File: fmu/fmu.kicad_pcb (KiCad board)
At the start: 4 copper layers, 103 parts, among them IC2 EFR32FG28B320F1024IM68-AR, J1 1054500101, J4 2213932-3, J5 2213932-3, J6 2213932-3, J7 2213932-3, U10 DMN3016LK3-13, U11 BQ7694203PFBR, U3 BNO055, U4 MCF8316A1VRGFR, U5 MCF8316A1VRGFR, U6 MCF8316A1VRGFR, U7 MCF8316A1VRGFR, U8 AR0130CSSC00SPBA0-DR, U9 MAX20075ATCA/V+

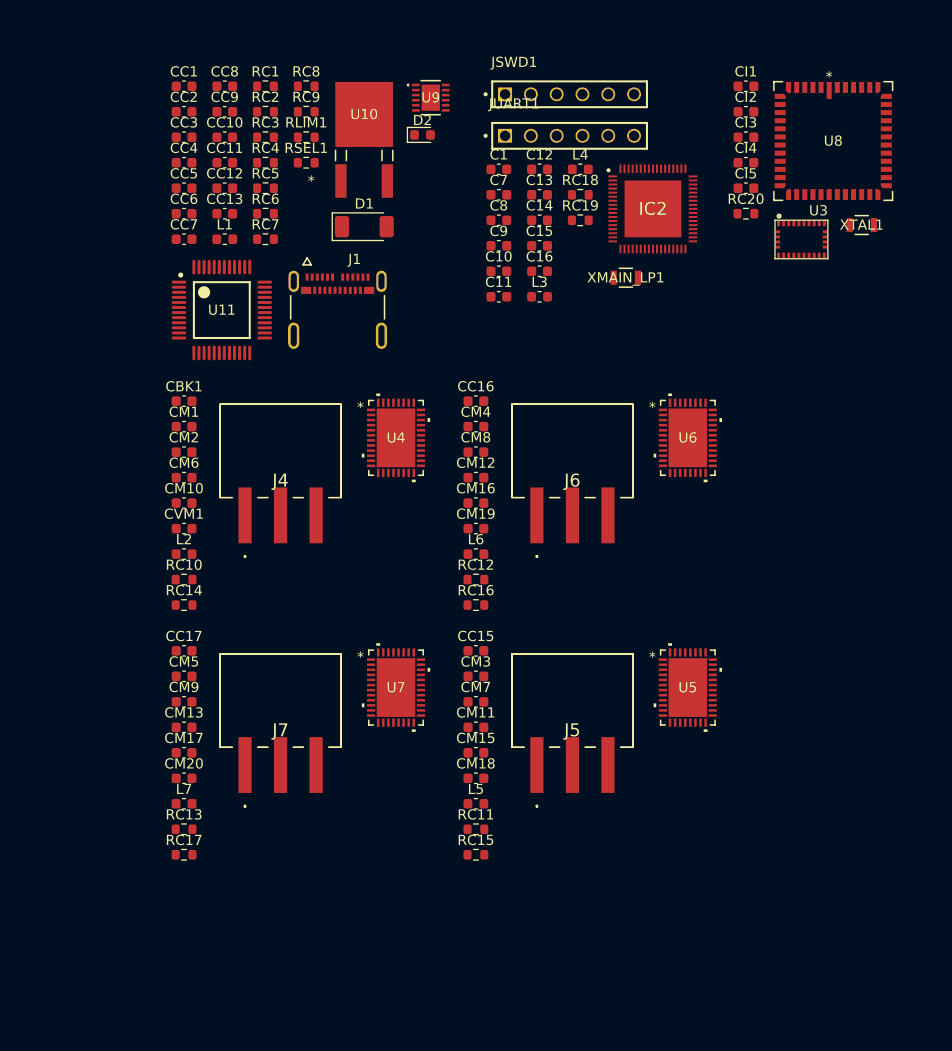
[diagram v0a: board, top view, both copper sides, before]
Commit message: Add voltage regulators
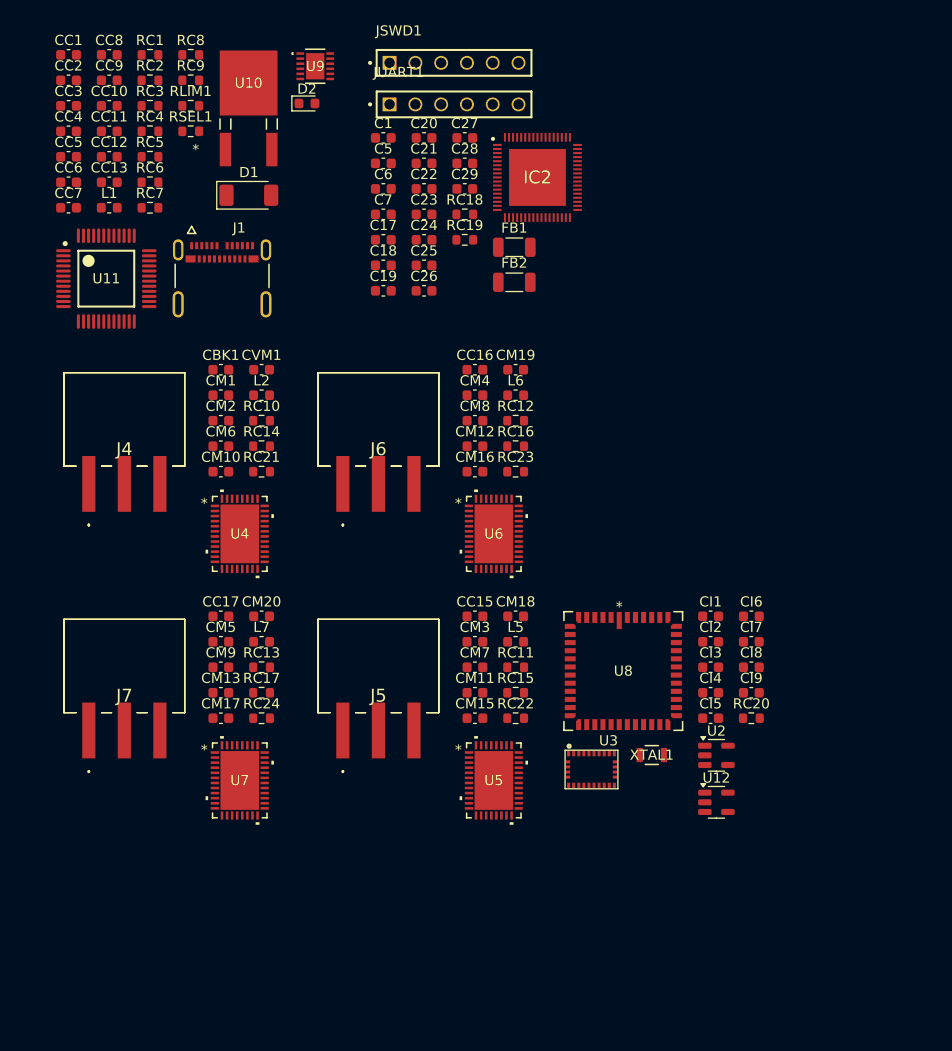
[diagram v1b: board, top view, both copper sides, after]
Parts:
- removed C10, C12, C8, C9: 100n, Capacitor_SMD:C_0603_1608Metric
- removed C11, C16: 12p, Capacitor_SMD:C_0603_1608Metric
- removed C13, C14: 1u, Capacitor_SMD:C_0603_1608Metric
- removed C15: 47n, Capacitor_SMD:C_0603_1608Metric
- removed L3: 10u, Inductor_SMD:L_0603_1608Metric
- removed L4: 15n, Inductor_SMD:L_0603_1608Metric
- removed XMAIN_LP1: 32KHz, ABS07:XTAL_ABS07-32.768KHZ-7-T_ABR
- added C17: 1u, Capacitor_SMD:C_0603_1608Metric, F.Cu at (136.6, 68.7)
- added C18: 0.1u, Capacitor_SMD:C_0603_1608Metric, F.Cu at (136.6, 71.2)
- added C19: 0.1u, Capacitor_SMD:C_0603_1608Metric, F.Cu at (136.6, 73.7)
- added C20: 1u, Capacitor_SMD:C_0603_1608Metric, F.Cu at (140.6, 58.6)
- added C21: 0.1u, Capacitor_SMD:C_0603_1608Metric, F.Cu at (140.6, 61.1)
- added C22: 1u, Capacitor_SMD:C_0603_1608Metric, F.Cu at (140.6, 63.6)
- added C23: 10u, Capacitor_SMD:C_0603_1608Metric, F.Cu at (140.6, 66.2)
- added C24: 0.1u, Capacitor_SMD:C_0603_1608Metric, F.Cu at (140.6, 68.7)
- added C25: 1u, Capacitor_SMD:C_0603_1608Metric, F.Cu at (140.6, 71.2)
- added C26: 100p, Capacitor_SMD:C_0603_1608Metric, F.Cu at (140.6, 73.7)
- added C27: 0.47u, Capacitor_SMD:C_0603_1608Metric, F.Cu at (144.6, 58.6)
- added C28: 100p, Capacitor_SMD:C_0603_1608Metric, F.Cu at (144.6, 61.1)
- added C29: 100p, Capacitor_SMD:C_0603_1608Metric, F.Cu at (144.6, 63.6)
- added C5: 0.1u, Capacitor_SMD:C_0603_1608Metric, F.Cu at (136.6, 61.1)
- added C6: 1u, Capacitor_SMD:C_0603_1608Metric, F.Cu at (136.6, 63.6)
- added CI6: 1u, Capacitor_SMD:C_0603_1608Metric, F.Cu at (172.8, 105.7)
- added CI7: 1u, Capacitor_SMD:C_0603_1608Metric, F.Cu at (172.8, 108.2)
- added CI8: 1u, Capacitor_SMD:C_0603_1608Metric, F.Cu at (172.8, 110.8)
- added CI9: 1u, Capacitor_SMD:C_0603_1608Metric, F.Cu at (172.8, 113.3)
- added FB1: 2512067007Y3, Inductor_SMD:L_1206_3216Metric, F.Cu at (149.5, 69.4)
- added FB2: BLM31PG330SN1L, Inductor_SMD:L_1206_3216Metric, F.Cu at (149.5, 72.8)
- added RC21: 10k, Resistor_SMD:R_0603_1608Metric, F.Cu at (124.6, 91.5)
- added RC22: 10k, Resistor_SMD:R_0603_1608Metric, F.Cu at (149.6, 115.8)
- added RC23: 10k, Resistor_SMD:R_0603_1608Metric, F.Cu at (149.6, 91.5)
- added RC24: 10k, Resistor_SMD:R_0603_1608Metric, F.Cu at (124.6, 115.8)
- added U12: LP5907MFX-2.8, Package_TO_SOT_SMD:SOT-23-5, F.Cu at (169.4, 124.0)
- added U2: LP5907MFX-1.8, Package_TO_SOT_SMD:SOT-23-5, F.Cu at (169.4, 119.4)
- C1: value 100p -> 10n
- C7: value 100n -> 1u
- moved U3 56.1 mm to (157.1, 120.8)
- moved XTAL1 56.1 mm to (163.0, 119.4)
- moved U8 56.1 mm to (160.2, 111.1)
- moved CI4 52.3 mm to (168.8, 113.3)
- moved CI1 52.3 mm to (168.8, 105.7)
- moved CI3 52.3 mm to (168.8, 110.8)
- moved CI2 52.3 mm to (168.8, 108.2)
- moved CI5 52.3 mm to (168.8, 115.8)
- moved RC20 49.7 mm to (172.8, 115.8)
- moved U6 21.3 mm to (147.4, 97.6)
- moved U5 21.2 mm to (147.4, 121.9)
- moved J5 19.4 mm to (136.1, 110.6)
- moved J6 19.4 mm to (136.1, 86.3)
- moved U4 18.1 mm to (122.4, 97.6)
- moved U7 17.9 mm to (122.4, 121.9)
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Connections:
- C1 pad 1: Net-(IC1-DEC3) -> GND
- C7 pad 1: +3.3V -> GND
- CBK1 pad 1: +3.3V -> GND
- CC10 pad 1: +3.3V -> GND
- CC2 pad 1: +3.3V -> GND
- CC3 pad 1: +3.3V -> GND
- CC4 pad 1: +3.3V -> GND
- CC5 pad 1: +3.3V -> GND
- CC6 pad 1: +3.3V -> GND
- CC7 pad 1: +3.3V -> GND
- CC8 pad 1: +3.3V -> GND
- CC9 pad 1: +3.3V -> GND
- CI1 pad 1: +3.3V -> GND
- CI2 pad 1: +3.3V -> GND
- CI3 pad 1: +3.3V -> GND
- CI4 pad 2: +3.3V -> GND
- CI5 pad 2: +3.3V -> GND
- CM10 pad 2: +3.3V -> GND
- CM11 pad 2: +3.3V -> GND
- CM12 pad 2: +3.3V -> GND
- CM13 pad 2: +3.3V -> GND
- CM18 pad 1: +3.3V -> GND
- CM19 pad 1: +3.3V -> GND
- CM20 pad 1: +3.3V -> GND
- CM6 pad 1: +3.3V -> GND
- CM7 pad 1: +3.3V -> GND
- CM8 pad 1: +3.3V -> GND
- CM9 pad 1: +3.3V -> GND
- IC2 pad 10: unconnected-(IC2-PC06-Pad10) -> /NFAULT3
- IC2 pad 11: unconnected-(IC2-PC07-Pad11) -> /NFAULT4
- IC2 pad 12: unconnected-(IC2-PC08-Pad12) -> /DIR1
- IC2 pad 13: unconnected-(IC2-PC09-Pad13) -> /DIR2
- IC2 pad 14: unconnected-(IC2-PC10-Pad14) -> /DIR3
- IC2 pad 15: unconnected-(IC2-PC11-Pad15) -> /DIR4
- IC2 pad 18: unconnected-(IC2-RESETN-Pad18) -> /mcu/RESET
- IC2 pad 19: unconnected-(IC2-RFVDD-Pad19) -> /mcu/RFVDD
- IC2 pad 20: unconnected-(IC2-RFVSS-Pad20) -> GND
- IC2 pad 25: unconnected-(IC2-PAVDD-Pad25) -> /mcu/PAVDD
- IC2 pad 28: unconnected-(IC2-PB03-Pad28) -> /mcu/UART_TXD
- IC2 pad 29: unconnected-(IC2-PB02-Pad29) -> /mcu/UART_RXD
- IC2 pad 3: unconnected-(IC2-PC00-Pad3) -> /PWM1
- IC2 pad 30: unconnected-(IC2-PB01-Pad30) -> /mcu/NBOOT_LOAD
- IC2 pad 31: unconnected-(IC2-PB00-Pad31) -> /mcu/IMU_INT
- IC2 pad 32: unconnected-(IC2-PA00-Pad32) -> /mcu/IMU_NRST
- IC2 pad 33: unconnected-(IC2-IOVDD_2-Pad33) -> +3.3V
- IC2 pad 34: unconnected-(IC2-PA01-Pad34) -> /mcu/SWCLK
- IC2 pad 35: unconnected-(IC2-PA02-Pad35) -> /mcu/SWDIO
- IC2 pad 36: unconnected-(IC2-PA03-Pad36) -> /mcu/SWO
- IC2 pad 37: unconnected-(IC2-PA04-Pad37) -> /FG1
- IC2 pad 38: unconnected-(IC2-PA05-Pad38) -> /FG2
- IC2 pad 39: unconnected-(IC2-PA06-Pad39) -> /FG3
- IC2 pad 4: unconnected-(IC2-PC01-Pad4) -> /PWM2
- IC2 pad 40: unconnected-(IC2-PA07-Pad40) -> /FG4
- IC2 pad 45: unconnected-(IC2-PA12-Pad45) -> /mcu/PIXCLK
- IC2 pad 46: unconnected-(IC2-PA13-Pad46) -> /mcu/FRAME_VALID
- IC2 pad 47: unconnected-(IC2-PA14-Pad47) -> /mcu/LINE_VALID
- IC2 pad 48: unconnected-(IC2-DECOUPLE-Pad48) -> Net-(IC2-DECOUPLE)
- IC2 pad 5: unconnected-(IC2-PC02-Pad5) -> /PWM3
- IC2 pad 50: unconnected-(IC2-VREGVDD-Pad50) -> +3.3V
- IC2 pad 51: unconnected-(IC2-VREGVSS-Pad51) -> GND
- IC2 pad 52: unconnected-(IC2-DVDD-Pad52) -> +3.3V
- IC2 pad 53: unconnected-(IC2-AVDD-Pad53) -> +3.3V
- IC2 pad 54: unconnected-(IC2-IOVDD_3-Pad54) -> +3.3V
- IC2 pad 55: unconnected-(IC2-PD15-Pad55) -> /mcu/SCL
- IC2 pad 56: unconnected-(IC2-PD14-Pad56) -> /mcu/SDA
- IC2 pad 57: unconnected-(IC2-PD13-Pad57) -> /mcu/DOUT11
- IC2 pad 58: unconnected-(IC2-PD12-Pad58) -> /mcu/DOUT10
- IC2 pad 59: unconnected-(IC2-PD11-Pad59) -> /mcu/DOUT9
- IC2 pad 6: unconnected-(IC2-IOVDD_1-Pad6) -> +3.3V
- IC2 pad 60: unconnected-(IC2-PD10-Pad60) -> /mcu/DOUT8
- IC2 pad 61: unconnected-(IC2-PD09-Pad61) -> /mcu/DOUT7
- IC2 pad 62: unconnected-(IC2-PD08-Pad62) -> /mcu/DOUT6
- IC2 pad 63: unconnected-(IC2-PD07-Pad63) -> /mcu/DOUT5
- IC2 pad 64: unconnected-(IC2-PD06-Pad64) -> /mcu/DOUT4
- IC2 pad 65: unconnected-(IC2-PD05-Pad65) -> /mcu/DOUT3
- IC2 pad 66: unconnected-(IC2-PD04-Pad66) -> /mcu/DOUT2
- IC2 pad 67: unconnected-(IC2-PD03-Pad67) -> /mcu/DOUT1
- IC2 pad 68: unconnected-(IC2-PD02-Pad68) -> /mcu/DOUT0
- IC2 pad 69: unconnected-(IC2-VSS-Pad69) -> GND
- IC2 pad 7: unconnected-(IC2-PC03-Pad7) -> /PWM4
- IC2 pad 8: unconnected-(IC2-PC04-Pad8) -> /NFAULT1
- IC2 pad 9: unconnected-(IC2-PC05-Pad9) -> /NFAULT2
- J1 pad A1: +3.3V -> GND
- J1 pad A12: +3.3V -> GND
- J1 pad B1: +3.3V -> GND
- J1 pad B12: +3.3V -> GND
- JSWD1 pad 02: unconnected-(JSWD1-Pad02) -> /mcu/SWO
- JSWD1 pad 05: unconnected-(JSWD1-Pad05) -> /mcu/RESET
- JSWD1 pad 06: +3.3V -> GND
- JUART1 pad 02: /mcu/UART_RTS -> unconnected-(JUART1-Pad02)
- JUART1 pad 05: /mcu/UART_CTS -> unconnected-(JUART1-Pad05)
- JUART1 pad 06: +3.3V -> GND
- RC10 pad 2: /motor1/NFAULT -> /NFAULT1
- RC11 pad 2: /motor2/NFAULT -> /NFAULT2
- RC12 pad 2: /motor3/NFAULT -> /NFAULT3
- RC13 pad 2: /motor4/NFAULT -> /NFAULT4
- RC14 pad 2: /motor1/FG -> /FG1
- RC15 pad 2: /motor2/FG -> /FG2
- RC16 pad 2: /motor3/FG -> /FG3
- RC17 pad 2: /motor4/FG -> /FG4
- RLIM1 pad 2: +3.3V -> GND
- RSEL1 pad 2: +3.3V -> GND
- U10 pad 2: +3.3V -> GND
- U3 pad 17: +3.3V -> GND
- U3 pad 18: +3.3V -> GND
- U3 pad 2: +3.3V -> GND
- U3 pad 25: +3.3V -> GND
- U3 pad 5: +3.3V -> GND
- U3 pad 6: +3.3V -> GND
- U4 pad 2: +3.3V -> GND
- U4 pad 21: +3.3V -> GND
- U4 pad 26: +3.3V -> GND
- U4 pad 28: /motor1/SPEED -> /PWM1
- U4 pad 29: /motor1/FG -> /FG1
- U4 pad 34: /motor1/DIR -> /DIR1
- U4 pad 35: /motor1/BRAKE -> Net-(U4-BRAKE)
- U4 pad 38: /motor1/CURRENT_SENS -> unconnected-(U4-SOX-Pad38)
- U4 pad 4: +3.3V -> GND
- U4 pad 40: /motor1/NFAULT -> /NFAULT1
- U4 pad 41: +3.3V -> GND
- U5 pad 2: +3.3V -> GND
- U5 pad 21: +3.3V -> GND
- U5 pad 26: +3.3V -> GND
- U5 pad 28: /motor2/SPEED -> /PWM2
- U5 pad 29: /motor2/FG -> /FG2
- U5 pad 34: /motor2/DIR -> /DIR2
- U5 pad 35: /motor2/BRAKE -> Net-(U5-BRAKE)
- U5 pad 38: /motor2/CURRENT_SENS -> unconnected-(U5-SOX-Pad38)
- U5 pad 4: +3.3V -> GND
- U5 pad 40: /motor2/NFAULT -> /NFAULT2
- U5 pad 41: +3.3V -> GND
- U6 pad 2: +3.3V -> GND
- U6 pad 21: +3.3V -> GND
- U6 pad 26: +3.3V -> GND
- U6 pad 28: /motor3/SPEED -> /PWM3
- U6 pad 29: /motor3/FG -> /FG3
- U6 pad 34: /motor3/DIR -> /DIR3
- U6 pad 35: /motor3/BRAKE -> Net-(U6-BRAKE)
- U6 pad 38: /motor3/CURRENT_SENS -> unconnected-(U6-SOX-Pad38)
- U6 pad 4: +3.3V -> GND
- U6 pad 40: /motor3/NFAULT -> /NFAULT3
- U6 pad 41: +3.3V -> GND
- U7 pad 2: +3.3V -> GND
- U7 pad 21: +3.3V -> GND
- U7 pad 26: +3.3V -> GND
- U7 pad 28: /motor4/SPEED -> /PWM4
- U7 pad 29: /motor4/FG -> /FG4
- U7 pad 34: /motor4/DIR -> /DIR4
- U7 pad 35: /motor4/BRAKE -> Net-(U7-BRAKE)
- U7 pad 38: /motor4/CURRENT_SENS -> unconnected-(U7-SOX-Pad38)
- U7 pad 4: +3.3V -> GND
- U7 pad 40: /motor4/NFAULT -> /NFAULT4
- U7 pad 41: +3.3V -> GND
- U8 pad 12: unconnected-(U8-PIXCLK-Pad12) -> /sensor/PIXCLK
- U8 pad 15: unconnected-(U8-FRAME_VALID-Pad15) -> /sensor/FRAME_VALID
- U8 pad 16: unconnected-(U8-LINE_VALID-Pad16) -> /sensor/LINE_VALID
- U8 pad 17: /DOUT11 -> /mcu/DOUT11
- U8 pad 18: /DOUT10 -> /mcu/DOUT10
- U8 pad 19: /DOUT9 -> /mcu/DOUT9
- U8 pad 2: +3.3V -> GND
- U8 pad 20: /DOUT8 -> /mcu/DOUT8
- U8 pad 21: /DOUT7 -> /mcu/DOUT7
- U8 pad 22: /DOUT6 -> /mcu/DOUT6
- U8 pad 23: /DOUT5 -> /mcu/DOUT5
- U8 pad 24: /DOUT4 -> /mcu/DOUT4
- U8 pad 25: /DOUT3 -> /mcu/DOUT3
- U8 pad 26: /DOUT2 -> /mcu/DOUT2
- U8 pad 27: /DOUT1 -> /mcu/DOUT1
- U8 pad 28: /DOUT0 -> /mcu/DOUT0
- U8 pad 38: +3.3V -> GND
- U8 pad 39: +3.3V -> GND
- U8 pad 42: +3.3V -> GND
- U8 pad 43: +3.3V -> GND
- U8 pad 47: +3.3V -> GND
- U8 pad 48: +3.3V -> GND
- U8 pad 5: +3.3V -> GND
- U8 pad 6: +3.3V -> GND

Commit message: Start wiring battery protector; mark charger as non-BOM
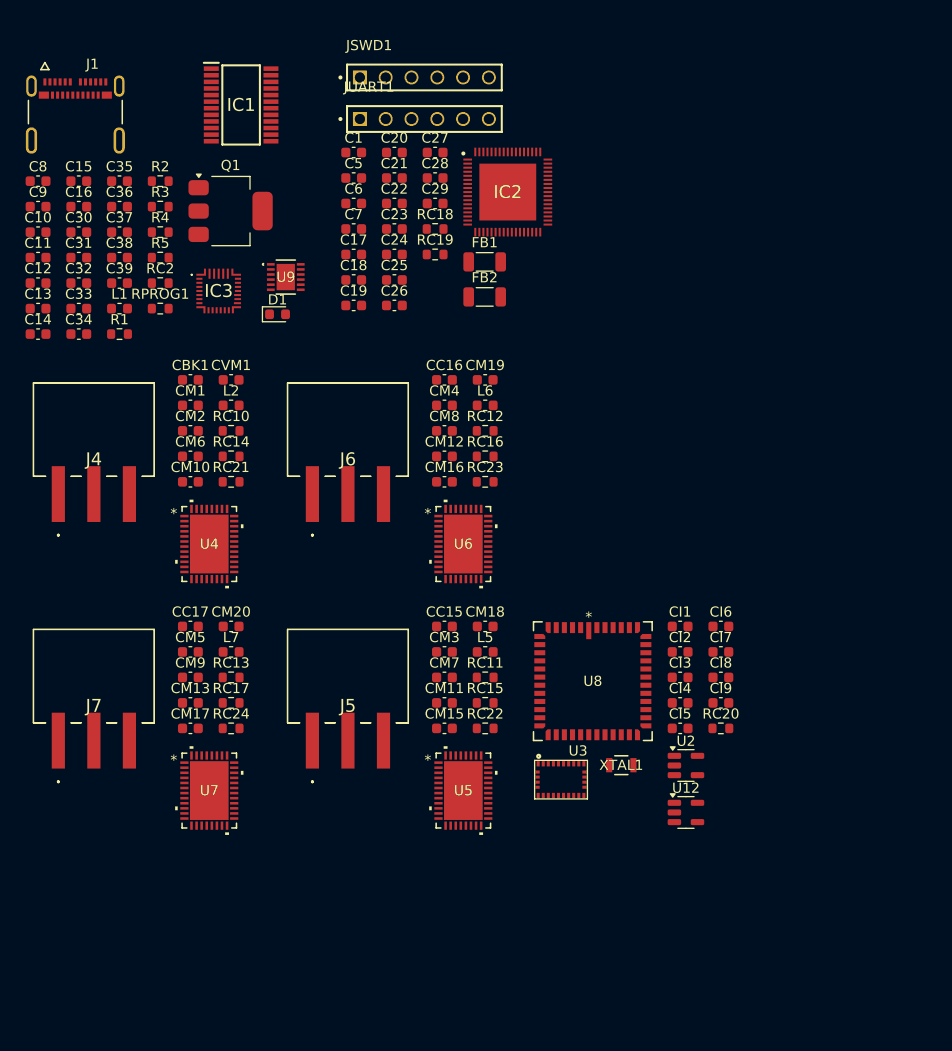
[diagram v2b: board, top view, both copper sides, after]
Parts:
- removed CC1: 0.1u, Capacitor_SMD:C_0603_1608Metric
- removed CC10: 1u, Capacitor_SMD:C_0603_1608Metric
- removed CC11, CC12: 0.22u, Capacitor_SMD:C_0603_1608Metric
- removed CC13: 0.047u, Capacitor_SMD:C_0603_1608Metric
- removed CC2, CC3: 0.015u, Capacitor_SMD:C_0603_1608Metric
- removed CC4, CC9: 10u, Capacitor_SMD:C_0603_1608Metric
- removed CC5, CC6: 4.7u, Capacitor_SMD:C_0603_1608Metric
- removed CC7, CC8: 47u, Capacitor_SMD:C_0603_1608Metric
- removed D2: LED, LED_SMD:LED_0603_1608Metric
- removed RC1, RC3: 10m, Resistor_SMD:R_0603_1608Metric
- removed RC4: 4.7, Resistor_SMD:R_0603_1608Metric
- removed RC5: 510, Resistor_SMD:R_0603_1608Metric
- removed RC6: 200k, Resistor_SMD:R_0603_1608Metric
- removed RC7: 220k, Resistor_SMD:R_0603_1608Metric
- removed RC8: 1k, Resistor_SMD:R_0603_1608Metric
- removed RC9: 470k, Resistor_SMD:R_0603_1608Metric
- removed RLIM1: 69800, Resistor_SMD:R_0603_1608Metric
- removed RSEL1: 8660, Resistor_SMD:R_0603_1608Metric
- removed U10: DMN3016LK3-13, DMN:TO-252_DIO
- removed U11: BQ7694203PFBR, BQ7694203:PFB0048A_N
- added C10: 47n, Capacitor_SMD:C_0603_1608Metric, F.Cu at (102.6, 67.9)
- added C11: 0.1u, Capacitor_SMD:C_0603_1608Metric, F.Cu at (102.6, 70.4)
- added C12: 10u, Capacitor_SMD:C_0603_1608Metric, F.Cu at (102.6, 72.9)
- added C13: 10u, Capacitor_SMD:C_0603_1608Metric, F.Cu at (102.6, 75.4)
- added C14: 10u, Capacitor_SMD:C_0603_1608Metric, F.Cu at (102.6, 77.9)
- added C15: 10u, Capacitor_SMD:C_0603_1608Metric, F.Cu at (106.6, 62.9)
- added C16: 10u, Capacitor_SMD:C_0603_1608Metric, F.Cu at (106.6, 65.4)
- added C30: 0.1u, Capacitor_SMD:C_0603_1608Metric, F.Cu at (106.6, 67.9)
- added C31: 10u, Capacitor_SMD:C_0603_1608Metric, F.Cu at (106.6, 70.4)
- added C32: 10u, Capacitor_SMD:C_0603_1608Metric, F.Cu at (106.6, 72.9)
- added C33: 10u, Capacitor_SMD:C_0603_1608Metric, F.Cu at (106.6, 75.4)
- added C34: 33u, Capacitor_SMD:C_0603_1608Metric, F.Cu at (106.6, 77.9)
- added C35: 33u, Capacitor_SMD:C_0603_1608Metric, F.Cu at (110.6, 62.9)
- added C36: 0.1u, Capacitor_SMD:C_0603_1608Metric, F.Cu at (110.6, 65.4)
- added C37: 47n, Capacitor_SMD:C_0603_1608Metric, F.Cu at (110.6, 67.9)
- added C38: 10u, Capacitor_SMD:C_0603_1608Metric, F.Cu at (110.6, 70.4)
- added C39: 10u, Capacitor_SMD:C_0603_1608Metric, F.Cu at (110.6, 72.9)
- added C8: 4.7u, Capacitor_SMD:C_0603_1608Metric, F.Cu at (102.6, 62.9)
- added C9: 47n, Capacitor_SMD:C_0603_1608Metric, F.Cu at (102.6, 65.4)
- added IC1: BQ7791500PWT, BQ77915:SOP65P640X120-24N, F.Cu at (122.6, 55.4)
- added IC3: BQ25798RQMR, BQ25798:BQ25798RQMR, F.Cu at (120.3, 73.7)
- added Q1: NDT3055L, Package_TO_SOT_SMD:SOT-223-3_TabPin2, F.Cu at (121.5, 65.8)
- added R1: 2.2k, Resistor_SMD:R_0603_1608Metric, F.Cu at (110.6, 77.9)
- added R2: 127k, Resistor_SMD:R_0603_1608Metric, F.Cu at (114.6, 62.9)
- added R3: 100, Resistor_SMD:R_0603_1608Metric, F.Cu at (114.6, 65.4)
- added R4: 5.1k, Resistor_SMD:R_0603_1608Metric, F.Cu at (114.6, 67.9)
- added R5: 5.1k, Resistor_SMD:R_0603_1608Metric, F.Cu at (114.6, 70.4)
- added RPROG1: 13.7k, Resistor_SMD:R_0603_1608Metric, F.Cu at (114.6, 75.4)
- D1: value PMEG4050EP -> LED; footprint Diode_SMD:D_SOD-128 -> LED_SMD:LED_0603_1608Metric
- RC2: value 10m -> 100k
- moved J1 21.7 mm to (106.2, 60.6)
- moved U9 21.0 mm to (127.0, 72.3)
- moved RC2 20.0 mm to (114.6, 72.9)
- moved D1 12.1 mm to (126.1, 76.0)
- moved L1 9.98 mm to (110.6, 75.4)
- moved C27 3.26 mm to (141.7, 60.1)
- moved JSWD1 3.26 mm to (140.6, 52.7)
- moved C28 3.26 mm to (141.7, 62.6)
- moved C29 3.26 mm to (141.7, 65.1)
- moved FB1 3.26 mm to (146.5, 70.8)
- moved FB2 3.26 mm to (146.5, 74.3)
- moved IC2 3.26 mm to (148.8, 64.0)
- moved JUART1 3.26 mm to (140.6, 56.8)
- moved RC18 3.26 mm to (141.7, 67.6)
- moved RC19 3.26 mm to (141.7, 70.1)
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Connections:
- D1 pad 1: /power/SYS -> Net-(D1-K)
- D1 pad 2: /power/BATT -> Net-(D1-A)
- J1 pad A5: unconnected-(J1-CC1-PadA5) -> Net-(J1-CC1)
- J1 pad A6: unconnected-(J1-D1+-PadA6) -> /power/D+
- J1 pad A7: unconnected-(J1-D1--PadA7) -> /power/D-
- J1 pad B5: unconnected-(J1-CC2-PadB5) -> Net-(J1-CC2)
- J1 pad B6: unconnected-(J1-D2+-PadB6) -> /power/D+
- J1 pad B7: unconnected-(J1-D2--PadB7) -> /power/D-
- J1 pad SH1: unconnected-(J1-SHIELD3-PadSH1) -> GND
- J1 pad SH2: unconnected-(J1-SHIELD4-PadSH2) -> GND
- J1 pad SH3: unconnected-(J1-SHIELD1-PadSH3) -> GND
- J1 pad SH4: unconnected-(J1-SHIELD2-PadSH4) -> GND
- L1 pad 1: /power/BST1 -> /power/SW2
- L1 pad 2: /power/BST2 -> /power/SW1
- RC2 pad 1: /power/CSINP -> Net-(IC3-ILIM_HIZ)
- RC2 pad 2: /power/VBUS -> GND
- U8 pad 1: unconnected-(U8-VDD_PLL-Pad1) -> +2V8
- U8 pad 12: /sensor/PIXCLK -> /mcu/PIXCLK
- U8 pad 15: /sensor/FRAME_VALID -> /mcu/FRAME_VALID
- U8 pad 16: /sensor/LINE_VALID -> /mcu/LINE_VALID
- U8 pad 3: unconnected-(U8-VDD-Pad3) -> +1V8
- U8 pad 33: unconnected-(U8-TRIGGER-Pad33) -> /sensor/TRIGGER
- U8 pad 34: unconnected-(U8-VDD-Pad34) -> +1V8
- U8 pad 4: unconnected-(U8-VDD-Pad4) -> +1V8
- U8 pad 40: unconnected-(U8-VAA_PIX-Pad40) -> +2V8
- U8 pad 41: unconnected-(U8-VAA_PIX-Pad41) -> +2V8
- U8 pad 44: unconnected-(U8-VAA-Pad44) -> +2V8
- U8 pad 45: unconnected-(U8-VAA-Pad45) -> +2V8
- U8 pad 46: unconnected-(U8-VAA-Pad46) -> +2V8
- U8 pad 7: unconnected-(U8-VDD_IO-Pad7) -> +1V8
- U8 pad 8: unconnected-(U8-VDD_IO-Pad8) -> +1V8

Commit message: BQ7791500 almost completed
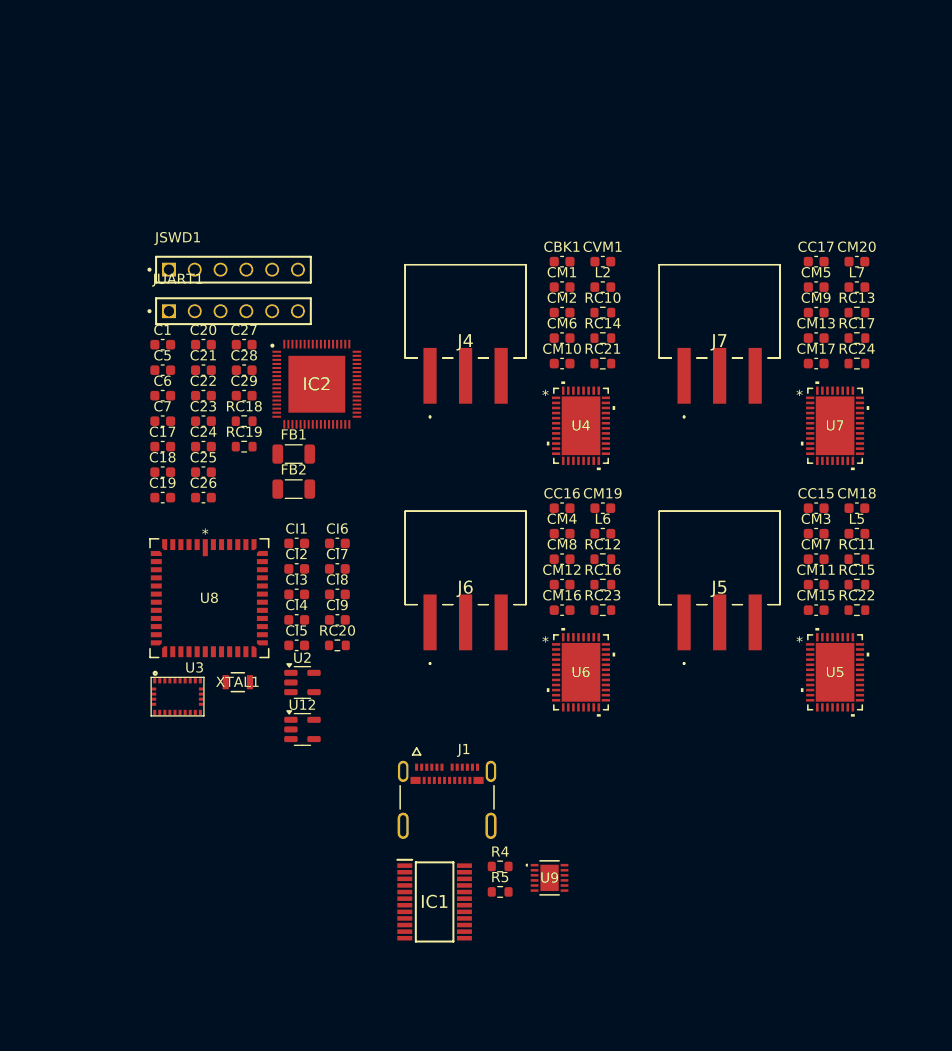
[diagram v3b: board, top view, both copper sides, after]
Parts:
- removed C10, C37, C9: 47n, Capacitor_SMD:C_0603_1608Metric
- removed C11, C30, C36: 0.1u, Capacitor_SMD:C_0603_1608Metric
- removed C12, C13, C14, C15, C16, C31, C32, C33, C38, C39: 10u, Capacitor_SMD:C_0603_1608Metric
- removed C34, C35: 33u, Capacitor_SMD:C_0603_1608Metric
- removed C8: 4.7u, Capacitor_SMD:C_0603_1608Metric
- removed D1: LED, LED_SMD:LED_0603_1608Metric
- removed IC3: BQ25798RQMR, BQ25798:BQ25798RQMR
- removed L1: 2.2u, Inductor_SMD:L_0603_1608Metric
- removed Q1: NDT3055L, Package_TO_SOT_SMD:SOT-223-3_TabPin2
- removed R1: 2.2k, Resistor_SMD:R_0603_1608Metric
- removed R2: 127k, Resistor_SMD:R_0603_1608Metric
- removed R3: 100, Resistor_SMD:R_0603_1608Metric
- removed RC2: 100k, Resistor_SMD:R_0603_1608Metric
- removed RPROG1: 13.7k, Resistor_SMD:R_0603_1608Metric
- moved IC1 80.8 mm to (141.6, 133.9)
- moved J1 76.8 mm to (142.8, 128.1)
- moved CC17 71.3 mm to (179.2, 70.8)
- moved CM13 71.3 mm to (179.2, 78.3)
- moved CM17 71.3 mm to (179.2, 80.8)
- moved CM5 71.3 mm to (179.2, 73.3)
- moved CM9 71.3 mm to (179.2, 75.8)
- moved J7 71.3 mm to (169.7, 75.7)
- moved U7 71.3 mm to (181.0, 87.0)
- moved CM20 71.3 mm to (183.2, 70.8)
- moved L7 71.3 mm to (183.2, 73.3)
- moved RC13 71.3 mm to (183.2, 75.8)
- moved RC17 71.3 mm to (183.2, 78.3)
- moved RC24 71.3 mm to (183.2, 80.8)
- moved R4 70.9 mm to (148.1, 130.4)
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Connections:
- IC1 pad 1: unconnected-(IC1-VDD-Pad1) -> Net-(IC1-VDD)
- IC1 pad 10: unconnected-(IC1-SRP-Pad10) -> GND
- IC1 pad 11: unconnected-(IC1-SRN-Pad11) -> Net-(IC1-SRN)
- IC1 pad 12: unconnected-(IC1-DSG-Pad12) -> Net-(IC1-DSG)
- IC1 pad 13: unconnected-(IC1-CHG-Pad13) -> Net-(IC1-CHG)
- IC1 pad 14: unconnected-(IC1-LD-Pad14) -> Net-(IC1-LD)
- IC1 pad 16: unconnected-(IC1-CBI-Pad16) -> GND
- IC1 pad 17: unconnected-(IC1-OCDP-Pad17) -> Net-(IC1-OCDP)
- IC1 pad 2: unconnected-(IC1-AVDD-Pad2) -> Net-(IC1-AVDD)
- IC1 pad 23: unconnected-(IC1-CTRC-Pad23) -> GND
- IC1 pad 24: unconnected-(IC1-CTRD-Pad24) -> GND
- IC1 pad 3: unconnected-(IC1-VC5-Pad3) -> Net-(IC1-VC3)
- IC1 pad 4: unconnected-(IC1-VC4-Pad4) -> Net-(IC1-VC3)
- IC1 pad 5: unconnected-(IC1-VC3-Pad5) -> Net-(IC1-VC3)
- IC1 pad 6: unconnected-(IC1-VC2-Pad6) -> Net-(IC1-VC2)
- IC1 pad 7: unconnected-(IC1-VC1-Pad7) -> Net-(IC1-VC1)
- IC1 pad 8: unconnected-(IC1-VC0-Pad8) -> Net-(IC1-VC0)
- IC1 pad 9: unconnected-(IC1-VSS-Pad9) -> GND

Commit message: Add SD Card reader
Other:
- board outline added: 80 x 80 mm
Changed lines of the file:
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@@
 		)
 	)
+	(gr_rect
+		(start 110.5 66.5)
+		(end 190.5 146.5)
+		(stroke
+			(width 0.05)
+			(type default)
+		)
+		(fill none)
+		(layer "Edge.Cuts")
+	)
 )
